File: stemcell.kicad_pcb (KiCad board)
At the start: 2 copper layers, 17.8 x 31.9 mm, 37 parts, among them J1 USB C Connector, J2 Left, J3 Right, J4 Down, SW1 Boot0, U1 STM32F4x1CxUx, U2 XC6220B331MR, Y1 HSE1 8Mhz 12pF

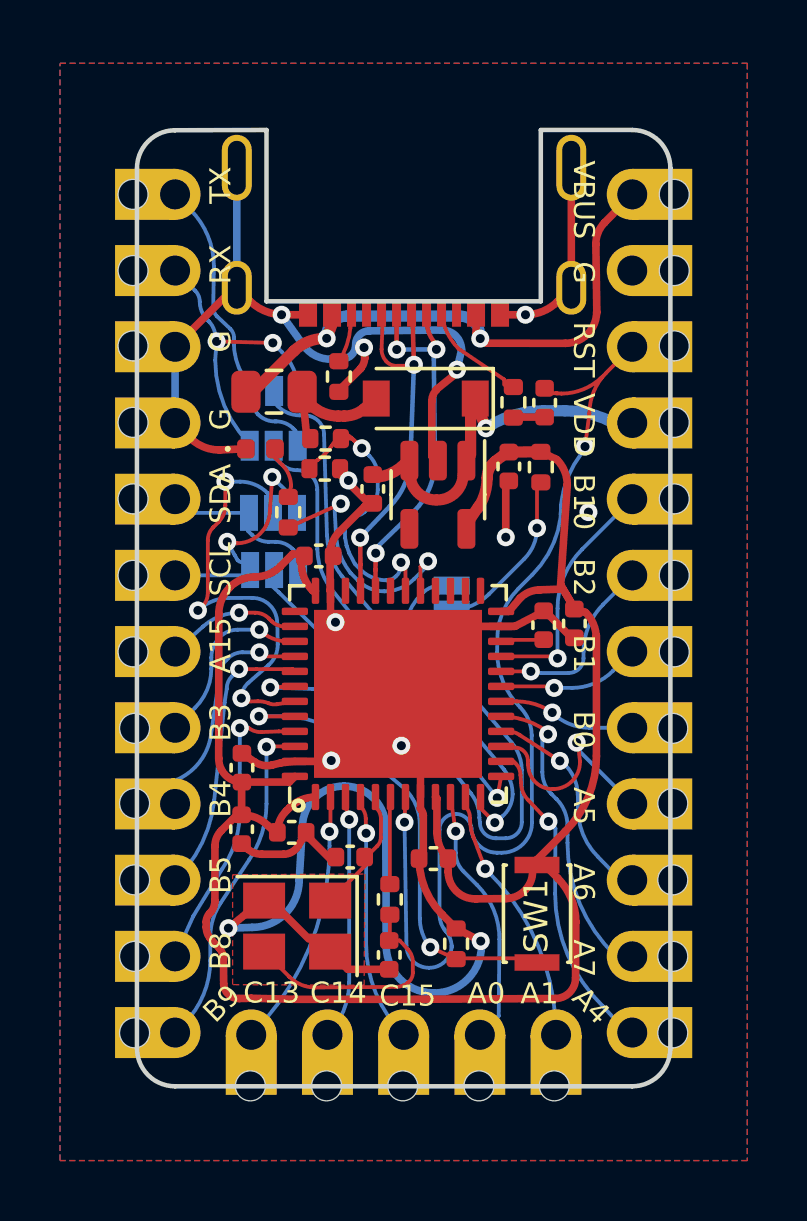
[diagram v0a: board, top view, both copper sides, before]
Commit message: updated to use type-c-31-m-12, since it's more commonly available
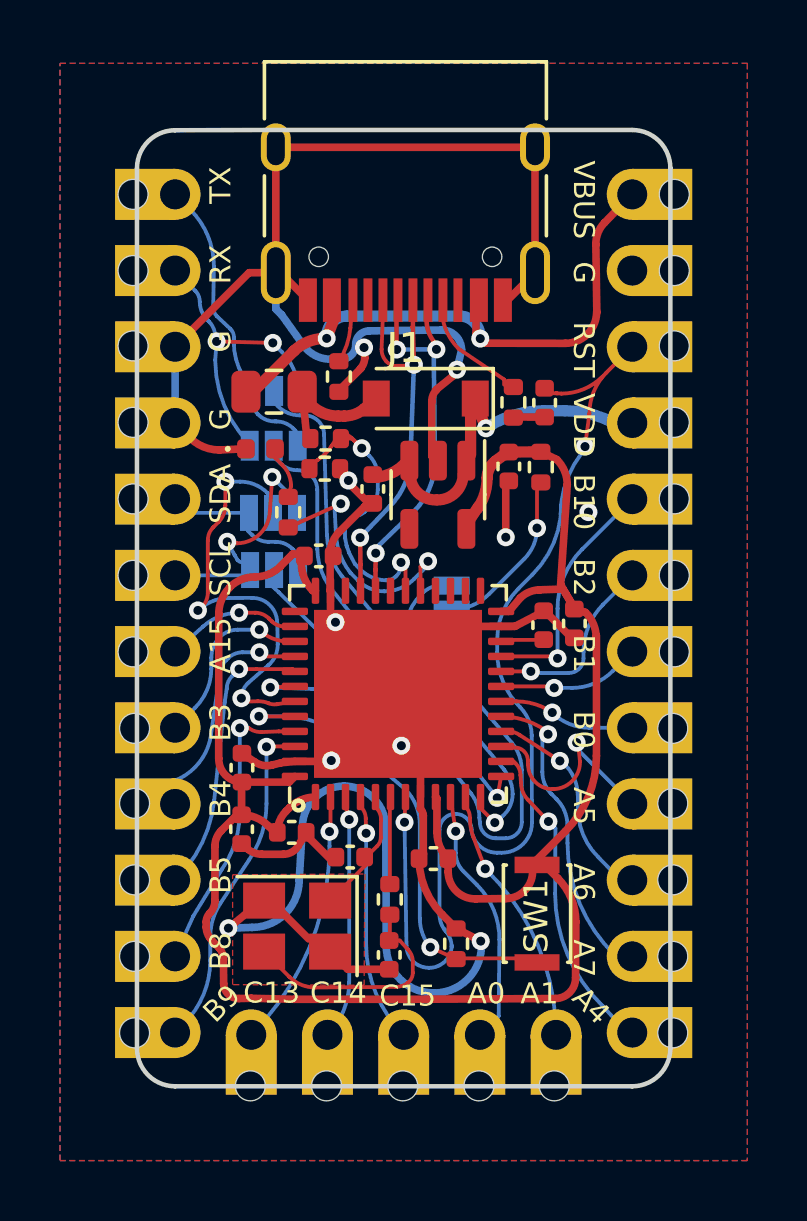
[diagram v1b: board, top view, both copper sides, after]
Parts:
- J1: footprint stemcell:USB-C-C168688 -> Connector_USB:USB_C_Receptacle_HRO_TYPE-C-31-M-12
- moved J1 2.47 mm to (100.2, 50.8), turned to 180 degrees
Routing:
- net GND: track 97.9 -> 107.5 mm, vias 12 -> 10
- net /USB_DP: track 12.0 -> 12.9 mm
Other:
- outline, holes or cut-outs redrawn

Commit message: added pre-soldered jumpers on the N position, can be cut with razor blade to remove
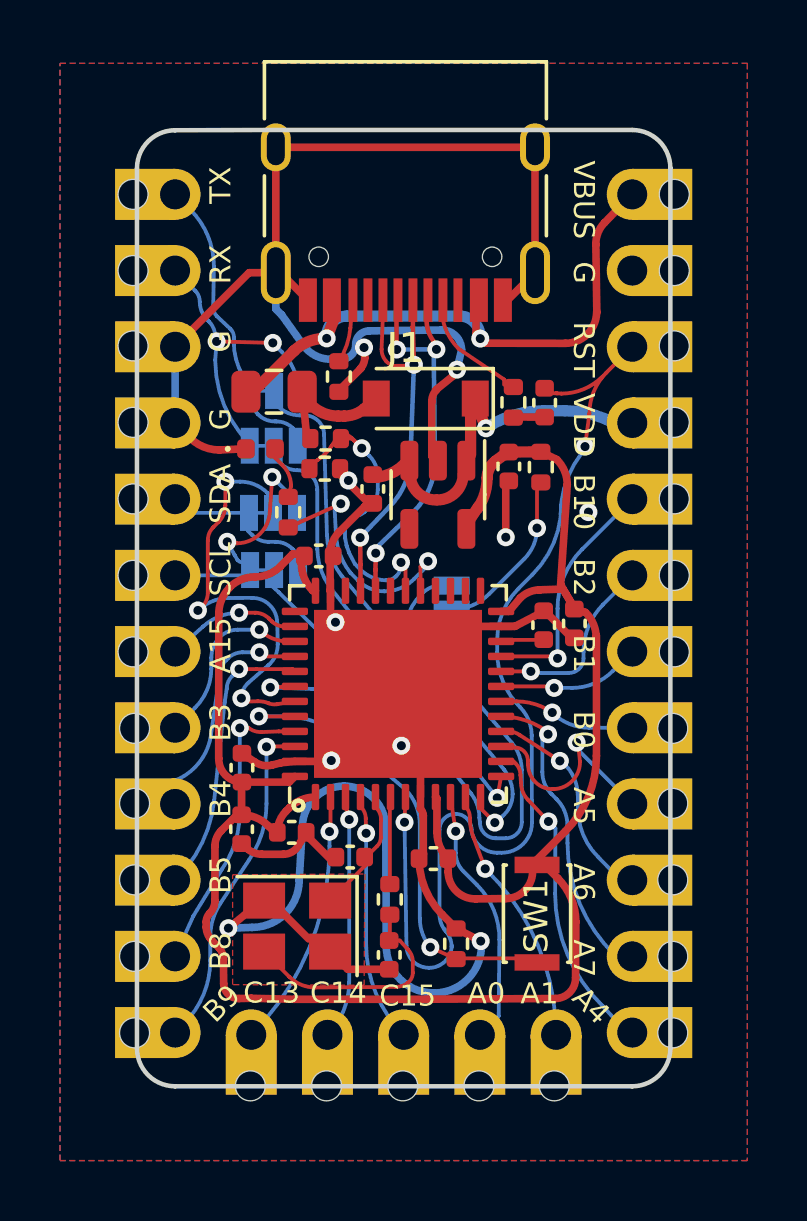
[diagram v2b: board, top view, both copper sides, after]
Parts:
- JP1, JP3: footprint stemcell:SOLDER_JUMPER_3 -> stemcell:SOLDER_JUMPER_3_2_3
- JP2, JP4: footprint stemcell:SOLDER_JUMPER_3 -> stemcell:SOLDER_JUMPER_3_1_2
